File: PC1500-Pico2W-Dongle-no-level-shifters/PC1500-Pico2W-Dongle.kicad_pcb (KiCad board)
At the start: 4 copper layers, 61 x 78 mm, 69 parts, among them J1 PC1500_60Pin_Connector, J2 microSD, J3 Spare GPIO (GP28), J5 GP2_Spare_IO, Q1 Si2333, Q2 MMBT2222A, U1 Pico2W, U2 AS6C62256-55SIN, U3 SLG46826G, U4 SLG46826G, U5 SC18IS602B, U6 TXS0108EPWR, U7 AP1117-ADJ, U8 TCA9406DC

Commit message: Add GreenPak bench-test/provisioning tools and no-level-shifters board variants
- GreenPakTester: standalone Pico 2 W bench-test firmware for the
  GreenPAK SLG46826V, with a VS-Code-extension-friendly project layout
  (Run/Flash/Serial-Monitor buttons via the Raspberry Pi Pico extension).
- GreenPak_Provision: standalone GreenPAK NVM provisioner, split out of
  RP2350's multi-target CMakeLists.txt into its own extension-friendly
  project for the same easy build/flash/serial-monitor workflow.
- PC1500-Pico2W-Dongle and PC1500-RP2350B-BLE: latest schematic/PCB
  edits, plus a new no-level-shifters KiCad variant of each board.
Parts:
- C1, C2, C3, C4, C5, C6, C7, C8: footprint C_0603_1608Metric -> Capacitor_SMD:C_0603_1608Metric
- D1: footprint D_SOD-123F -> Diode_SMD:D_SOD-123F
- J3, JP1, JP2: footprint PinHeader_1x02_P2.54mm_Vertical -> Connector_PinHeader_2.54mm:PinHeader_1x02_P2.54mm_Vertical
- J5: footprint PinHeader_1x03_P2.54mm_Vertical -> Connector_PinHeader_2.54mm:PinHeader_1x03_P2.54mm_Vertical
- R1: value 9.1k -> 330; footprint R_0603_1608Metric -> Resistor_SMD:R_0201_0603Metric
- R2: value 3.3k -> 910; footprint R_0603_1608Metric -> Resistor_SMD:R_0201_0603Metric
- U7: footprint SOT-223-3_TabPin2 -> Package_TO_SOT_SMD:SOT-223-3_TabPin2
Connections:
- C1 pad 1: +BATT -> unconnected-(C1-Pad1)
- C1 pad 2: GND -> unconnected-(C1-Pad2)
- C2 pad 1: VGG -> unconnected-(C2-Pad1)
- C2 pad 2: GND -> unconnected-(C2-Pad2)
- C6 pad 1: 3V3 -> unconnected-(C6-Pad1)
- C6 pad 2: GND -> unconnected-(C6-Pad2)
- C7 pad 2: GND -> unconnected-(C7-Pad2)
- C8 pad 1: 3V3 -> unconnected-(C8-Pad1)
- C8 pad 2: GND -> unconnected-(C8-Pad2)
- Q1 pad 1: GATE_NODE -> (no net)
- Q1 pad 2: VGG -> (no net)
- Q1 pad 3: VSYS_SW -> (no net)
- Q2 pad 1: Q2_BASE -> (no net)
- Q2 pad 2: GND -> (no net)
- Q2 pad 3: GATE_NODE -> (no net)
- U4 pad 2: (no net) -> unconnected-(U4-IO13-Pad2)
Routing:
- net GND: track 73.9 -> 68.6 mm, vias 31 -> 27
- net unconnected-(C6-Pad2): track 0.00 -> 1.42 mm, vias 0 -> 1
- net unconnected-(C8-Pad2): track 0.00 -> 1.30 mm, vias 0 -> 1
- net unconnected-(C2-Pad2): track 0.00 -> 1.29 mm, vias 0 -> 1
- net unconnected-(C1-Pad2): track 0.00 -> 1.28 mm, vias 0 -> 1

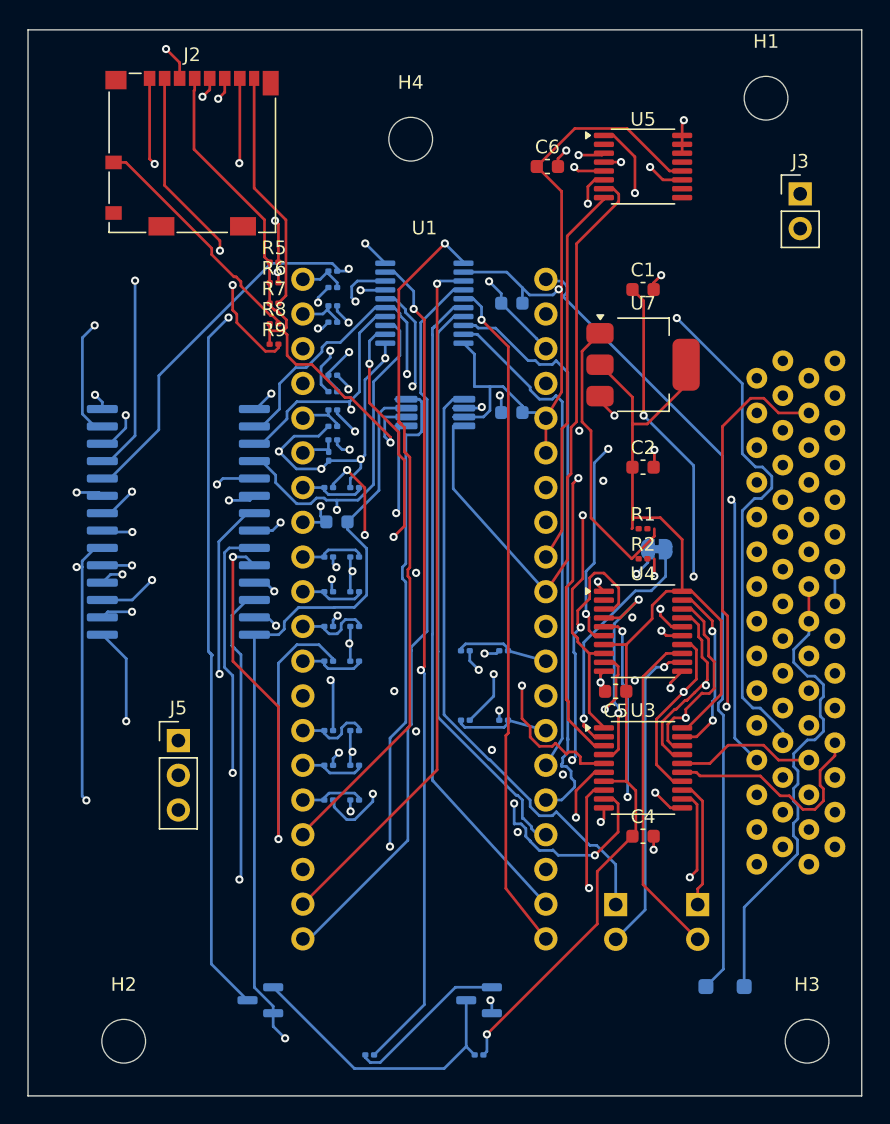
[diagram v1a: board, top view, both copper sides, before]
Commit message: Pico2W-Dongle-no-level-shifters: I2C pull-ups, cap fixes, SDA1/SCL1 rename, hand-routing
Schematic: R11-R14 I2C pull-up resistors (2K on VGG for SDA_GP/SCL_GP,
1.5K on 3V3 for SDA/SCL), C1/C2/C6/C7/C8 capacitor connections fixed
(were fully or partially unwired), JP1/JP2 renamed to SDA1/SCL1 to
match user's PCB-side silkscreen relabeling.

PCB: C1/C2/C6 net assignments patched to match; SDA1/SCL1 footprint
references renamed to match; user's manual routing/silkscreen fixes.

Known state: 0 unconnected nets, but 100 DRC violations remain (mostly
track_width squeeze escaping fine-pitch GreenPAK/SD-bridge pins, plus
some clearance/silk) -- not yet fab-clean, captured here as a checkpoint.
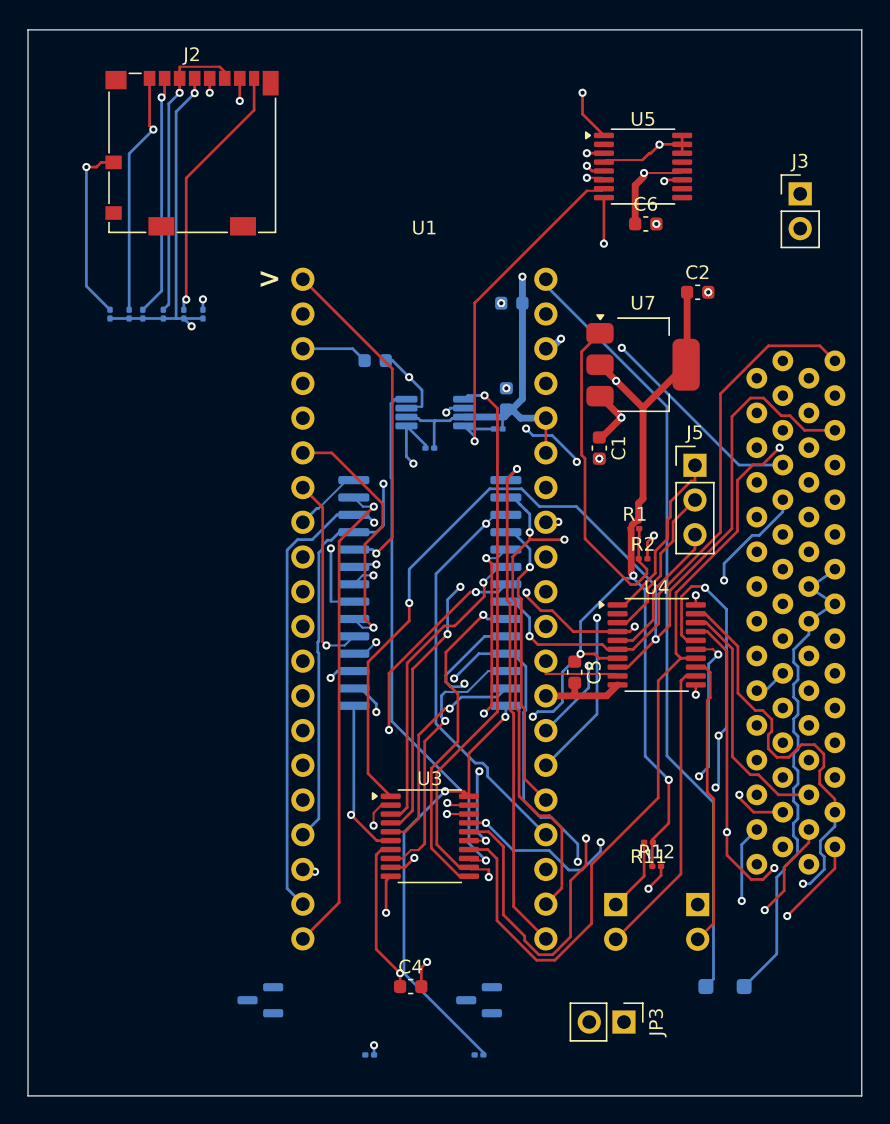
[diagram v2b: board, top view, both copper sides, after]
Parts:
- removed H1, H2, H3, H4: MountingHole_3.2mm_M3, MountingHole_3.2mm_M3
- removed Jumper1: Jumper_2_Bridged, Jumper:SolderJumper-2_P1.3mm_Bridged_RoundedPad1.0x1.5mm
- removed R15, R17, R19, R21, R23, R25, R27, R29, R31, R33, R35, R37, R39: 10k, Resistor_SMD:R_0201_0603Metric
- removed R16, R18, R20, R22, R24, R26, R28, R30, R32, R34, R36, R38: 4.7k, Resistor_SMD:R_0201_0603Metric
- removed U6: TXS0108EPWR, Package_SO:TSSOP-20_4.4x6.5mm_P0.65mm
- added JP3: 1500A, Connector_PinHeader_2.54mm:PinHeader_1x02_P2.54mm_Vertical, F.Cu at (40.6, 72.6)
- R10: value 4.7k -> 10k
- R11: value 10k -> 2K; moved to F.Cu
- R12: value 4.7k -> 2K; moved to F.Cu
- R13: value 10k -> 1.5K
- R14: value 4.7k -> 1.5K
- R5, R6, R7, R8, R9: moved to B.Cu
- moved R12 47.4 mm to (43.0, 61.2), turned to 0 degrees
- moved R11 46.7 mm to (42.4, 59.5)
- moved J5 42.8 mm to (45.8, 31.9)
- moved C4 20.2 mm to (25.0, 70.0)
- moved U2 19.1 mm to (26.4, 41.2)
- moved U3 16.4 mm to (26.4, 59.0)
- moved R10 15.2 mm to (4.40, 20.8), turned to -90 degrees
- moved R13 14.4 mm to (31.4, 29.2)
- moved C2 13.4 mm to (46.0, 19.2)
- moved C3 12.1 mm to (22.4, 24.2)
- moved C1 12.0 mm to (38.8, 30.6), turned to -90 degrees
- moved R8 12.0 mm to (3.00, 20.8), turned to 90 degrees
- moved R5 10.3 mm to (5.40, 20.8), turned to 90 degrees
- moved R14 8.88 mm to (26.4, 30.6)
- moved R6 8.42 mm to (6.90, 20.8), turned to 90 degrees
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- renumbered JP2 to SCL1, JP1 to SDA1
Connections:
- C1 pad 1: unconnected-(C1-Pad1) -> +BATT
- C1 pad 2: unconnected-(C1-Pad2) -> GND
- C2 pad 1: unconnected-(C2-Pad1) -> VGG
- C2 pad 2: unconnected-(C2-Pad2) -> GND
- C6 pad 1: unconnected-(C6-Pad1) -> 3V3
- C6 pad 2: unconnected-(C6-Pad2) -> GND
- C7 pad 2: unconnected-(C7-Pad2) -> GND
- C8 pad 1: unconnected-(C8-Pad1) -> 3V3
- C8 pad 2: unconnected-(C8-Pad2) -> GND
- J2 pad 1: SD_CS -> Net-(J2-CD/DAT3)
- J2 pad 2: SD_MOSI -> SD_CS
- J2 pad 3: GND -> SD_MOSI
- J2 pad 6: GND -> SD_MOSI
- R10 pad 1: AD0 -> Net-(J2-CD/DAT3)
- R10 pad 2: AD0_PICO -> 3V3
- R11 pad 1: AD0_PICO -> VGG
- R11 pad 2: GND -> SDA_GP
- R12 pad 1: AD1 -> VGG
- R12 pad 2: AD1_PICO -> SCL_GP
- R13 pad 1: AD1_PICO -> 3V3
- R13 pad 2: GND -> SDA
- R14 pad 1: AD2 -> 3V3
- R14 pad 2: AD2_PICO -> SCL
- U1 pad 1: AD0_PICO -> AD0
- U1 pad 10: AD7_PICO -> AD7
- U1 pad 11: AD8_PICO -> AD8
- U1 pad 12: AD9_PICO -> AD9
- U1 pad 14: AD10_PICO -> AD10
- U1 pad 15: AD11_PICO -> AD11
- U1 pad 16: AD12_PICO -> AD12
- U1 pad 17: D0_LV -> D0
- U1 pad 19: D1_LV -> D1
- U1 pad 2: AD1_PICO -> AD1
- U1 pad 20: D2_LV -> D2
- U1 pad 21: D3_LV -> D3
- U1 pad 22: D4_LV -> D4
- U1 pad 24: D5_LV -> D5
- U1 pad 25: D6_LV -> D6
- U1 pad 26: D7_LV -> D7
- U1 pad 27: TRIG_RD_PICO -> TRIG_RD
- U1 pad 29: TRIG_WR_PICO -> TRIG_WR
- U1 pad 4: AD2_PICO -> AD2
- U1 pad 5: AD3_PICO -> AD3
- U1 pad 6: AD4_PICO -> AD4
- U1 pad 7: AD5_PICO -> AD5
- U1 pad 9: AD6_PICO -> AD6
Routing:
- net VSYS_SW: track 78.1 -> 0.00 mm, vias 1 -> 0
- net D2_LV: track 54.1 -> 0.00 mm
- net D1_LV: track 51.5 -> 0.00 mm, vias 1 -> 0
- net D0_LV: track 50.8 -> 0.00 mm, vias 1 -> 0
- net D3_LV: track 49.7 -> 0.00 mm, vias 1 -> 0
- net D4_LV: track 48.4 -> 0.00 mm
- net AD4: track 103.3 -> 58.3 mm, vias 3 -> 2
- net D6_LV: track 42.9 -> 0.00 mm
- net D5_LV: track 42.8 -> 0.00 mm
- net GREENPAK2_IO12: track 51.6 -> 11.7 mm, vias 3 -> 0
- net SRAM_A14: track 51.6 -> 11.7 mm, vias 2 -> 1
- net GREENPAK2_IO10: track 49.9 -> 10.7 mm, vias 3 -> 0
- net SRAM_A13: track 58.0 -> 20.0 mm, vias 2 -> 1
- net D7_LV: track 36.6 -> 0.00 mm
- net DME0: track 41.6 -> 77.2 mm, vias 1 -> 2
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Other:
- board text added: ">"
